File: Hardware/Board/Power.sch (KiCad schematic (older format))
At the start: 0 parts

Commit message: Schaltregler Design fertig gestellt, Datenblätter hinzu gefügt.
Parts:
- added C?: 22nF, symbol Device:C
- added C? (x5): 2u2, symbol Device:C
- added C? (x5): 100nF, symbol Device:C
- added C? (x4): 22uF, symbol Device:C
- added C?: 10uF, symbol Device:C
- added C? (x3): 5n6, symbol Device:C
- added C? (x2): 100n, symbol Device:C
- added C?: 4u7, symbol Device:C
- added C? (x2): 47u, symbol Device:C
- added C?: 1u, symbol Device:C
- added C?: 10u, symbol Device:C
- added F?: KFZ 5A, symbol Device:Fuse
- added L?: 10uH, symbol Device:L
- added L? (x3): 15uH, symbol Device:L
- added L?: L_Core_Ferrite, symbol Device:L_Core_Ferrite
- added Q? (x3): Q_NMOS_DGS, symbol Device:Q_NMOS_DGS
- added R?: 105k, symbol Device:R
- added R?: 22k6, symbol Device:R
- added R? (x2): 4r7, symbol Device:R
- added R? (x3): 10k, symbol Device:R
- added R? (x6): 40k2, symbol Device:R
- added R?: 178k, symbol Device:R
- added R?: 39k, symbol Device:R
- added R? (x2): 86k6, symbol Device:R
- added R? (x2): 32k4, symbol Device:R
- added R?: 432k, symbol Device:R
- added R?: 3M3, symbol Device:R
- added R?: 49k9, symbol Device:R
- added U? (x3): MAX17572, Package_DFN_QFN:DFN-12-1EP_3x3mm_P0.5mm_EP2.05x2.86mm, symbol Regulator_Switching:MAX17572
- added U?: MAX17574, Package_DFN_QFN:QFN-24-1EP_4x5mm_P0.5mm_EP2.65x3.65mm, symbol Regulator_Switching:MAX17574
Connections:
- new net: C?.2, U?.10 (BST) (x3)
- new net: C?.1, L?.1, U?.11 (LX) (x3)
- new net: R?.1, R?.2, U?.2 (EN/UVLO)
- new net: C?.1, U?.4 (SS) (x3)
- new net: R?.1, U?.6 (RT/SYNC) (x3)
- new net: R?.1, R?.2, U?.7 (FB) (x3)
- new net: Q?.1 (D), R?.2, U?.2 (EN/UVLO) (x2)
- new net: C?.2, U?.5 (VCC)
- new net: C?.1, R?.2, U?.9 (EXTVCC)
- new net: C?.1, L?.1, U?.1 (LX), U?.23 (LX), U?.24 (LX)
- new net: Q?.1 (D), R?.2, U?.10 (EN/UVLO)
- new net: C?.2, U?.12 (VCC)
- new net: C?.1, U?.16 (SS)
- new net: R?.1, R?.2, U?.18 (FB)
- new net: R?.1, U?.19 (RT)
- new net: R?.2, U?.20 (EXTVCC)
- new net: C?.2, U?.22 (BST)
- new net: Q?.2 (G), R?.1 (x3)
- new net: F?.2, L?.1
- new net +3.3VA: C?.1, L?.2, R?.1
- new net +3V3: C?.1, L?.2, R?.1
- new net +5V: C?.1, L?.2, R?.1, R?.1
- new net +5VD: C?.1, C?.1, C?.1, L?.2, R?.1, R?.1
- new net +BATT: C?.1, C?.1, C?.1, C?.1, C?.1, C?.1, C?.1, F?.1, R?.1, R?.1, R?.1, R?.1, U?.1 (VIN), U?.1 (VIN), U?.1 (VIN), U?.5 (VIN), U?.6 (VIN), U?.7 (VIN), U?.9 (VIN)
- new net 3VA_EN: R?.2
- new net 5V_EN: R?.2
- new net 5V_Raspi_EN: R?.2
- new net DC_Input: C?.1, C?.1, L?.2
- new net GND: C?.1, C?.1, C?.2, C?.2, C?.2, C?.2, C?.2, C?.2, C?.2, C?.2, C?.2, C?.2, C?.2, C?.2, C?.2, C?.2, C?.2, C?.2, C?.2, C?.2, C?.2, C?.2, Q?.3 (S), Q?.3 (S), Q?.3 (S), R?.2, R?.2, R?.2, R?.2, R?.2, R?.2, R?.2, R?.2, R?.2, U?.11 (PGND), U?.12 (PGND), U?.12 (PGND), U?.12 (PGND), U?.13 (EP), U?.13 (EP), U?.13 (EP), U?.2 (PGND), U?.21 (SGND), U?.25 (EP), U?.3 (PGND), U?.5 (VCC), U?.5 (VCC), U?.8 (GND), U?.8 (GND), U?.8 (GND), U?.9 (EXTVCC), U?.9 (EXTVCC)
- new net PWR_Reset: U?.3 (~RESET)
- no-connect marks 0 -> 4

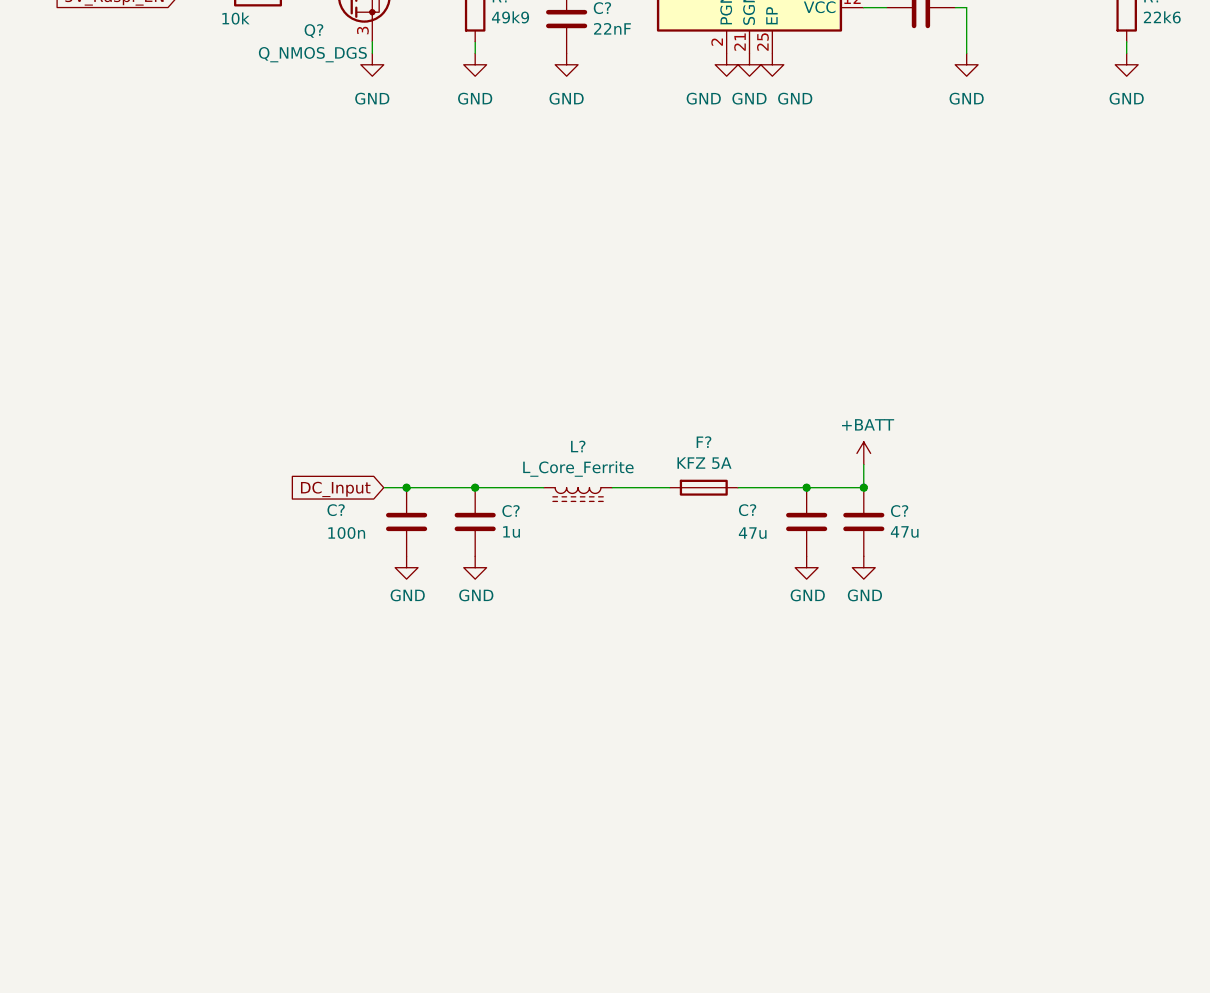
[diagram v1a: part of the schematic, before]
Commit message: FTDI EVE Touch hinzugefügt
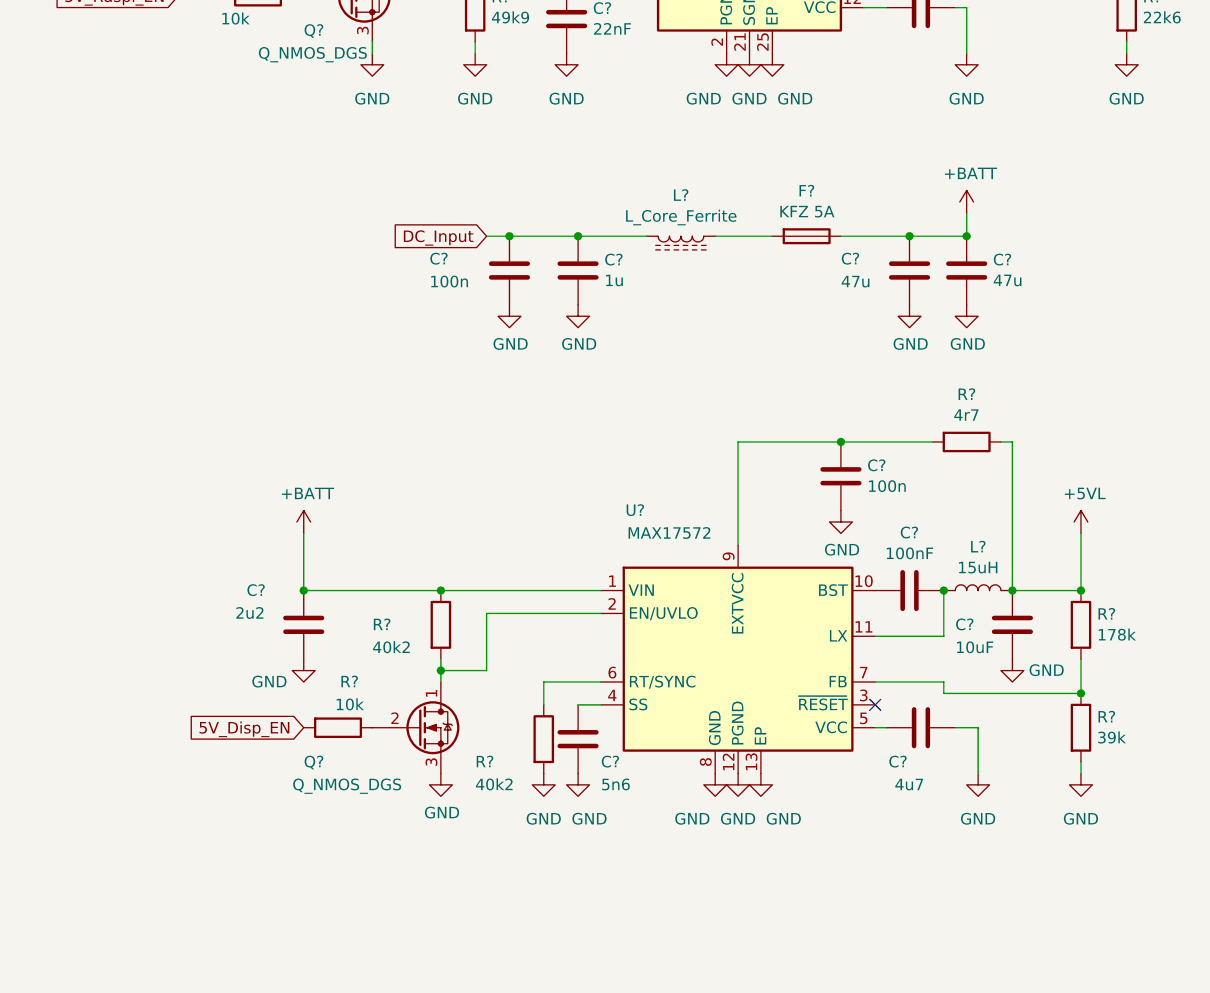
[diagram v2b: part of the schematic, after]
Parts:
- added C?: 10uF, symbol Device:C
- added C?: 5n6, symbol Device:C
- added C?: 100nF, symbol Device:C
- added C?: 2u2, symbol Device:C
- added C?: 100n, symbol Device:C
- added C?: 4u7, symbol Device:C
- added L?: 15uH, symbol Device:L
- added Q?: Q_NMOS_DGS, symbol Device:Q_NMOS_DGS
- added R?: 178k, symbol Device:R
- added R?: 39k, symbol Device:R
- added R? (x2): 40k2, symbol Device:R
- added R?: 4r7, symbol Device:R
- added R?: 10k, symbol Device:R
- added U?: MAX17572, Package_DFN_QFN:DFN-12-1EP_3x3mm_P0.5mm_EP2.05x2.86mm, symbol Regulator_Switching:MAX17572
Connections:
- net +BATT: now also C?.1, R?.1, U?.1 (VIN)
- net GND: now also C?.1, C?.2, C?.2, C?.2, C?.2, Q?.3 (S), R?.2, R?.2, U?.12 (PGND), U?.13 (EP), U?.8 (GND)
- new net: C?.1, L?.1, U?.11 (LX)
- new net: R?.1, R?.2, U?.7 (FB)
- new net: C?.1, U?.4 (SS)
- new net: C?.2, U?.10 (BST)
- new net: R?.1, U?.6 (RT/SYNC)
- new net: C?.1, R?.2, U?.9 (EXTVCC)
- new net: Q?.1 (D), R?.2, U?.2 (EN/UVLO)
- new net: C?.2, U?.5 (VCC)
- new net: Q?.2 (G), R?.1
- new net +5VL: C?.1, L?.2, R?.1, R?.1
- new net 5V_Disp_EN: R?.2
- no-connect marks 4 -> 5
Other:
- moved on the sheet: C?, F?, L?

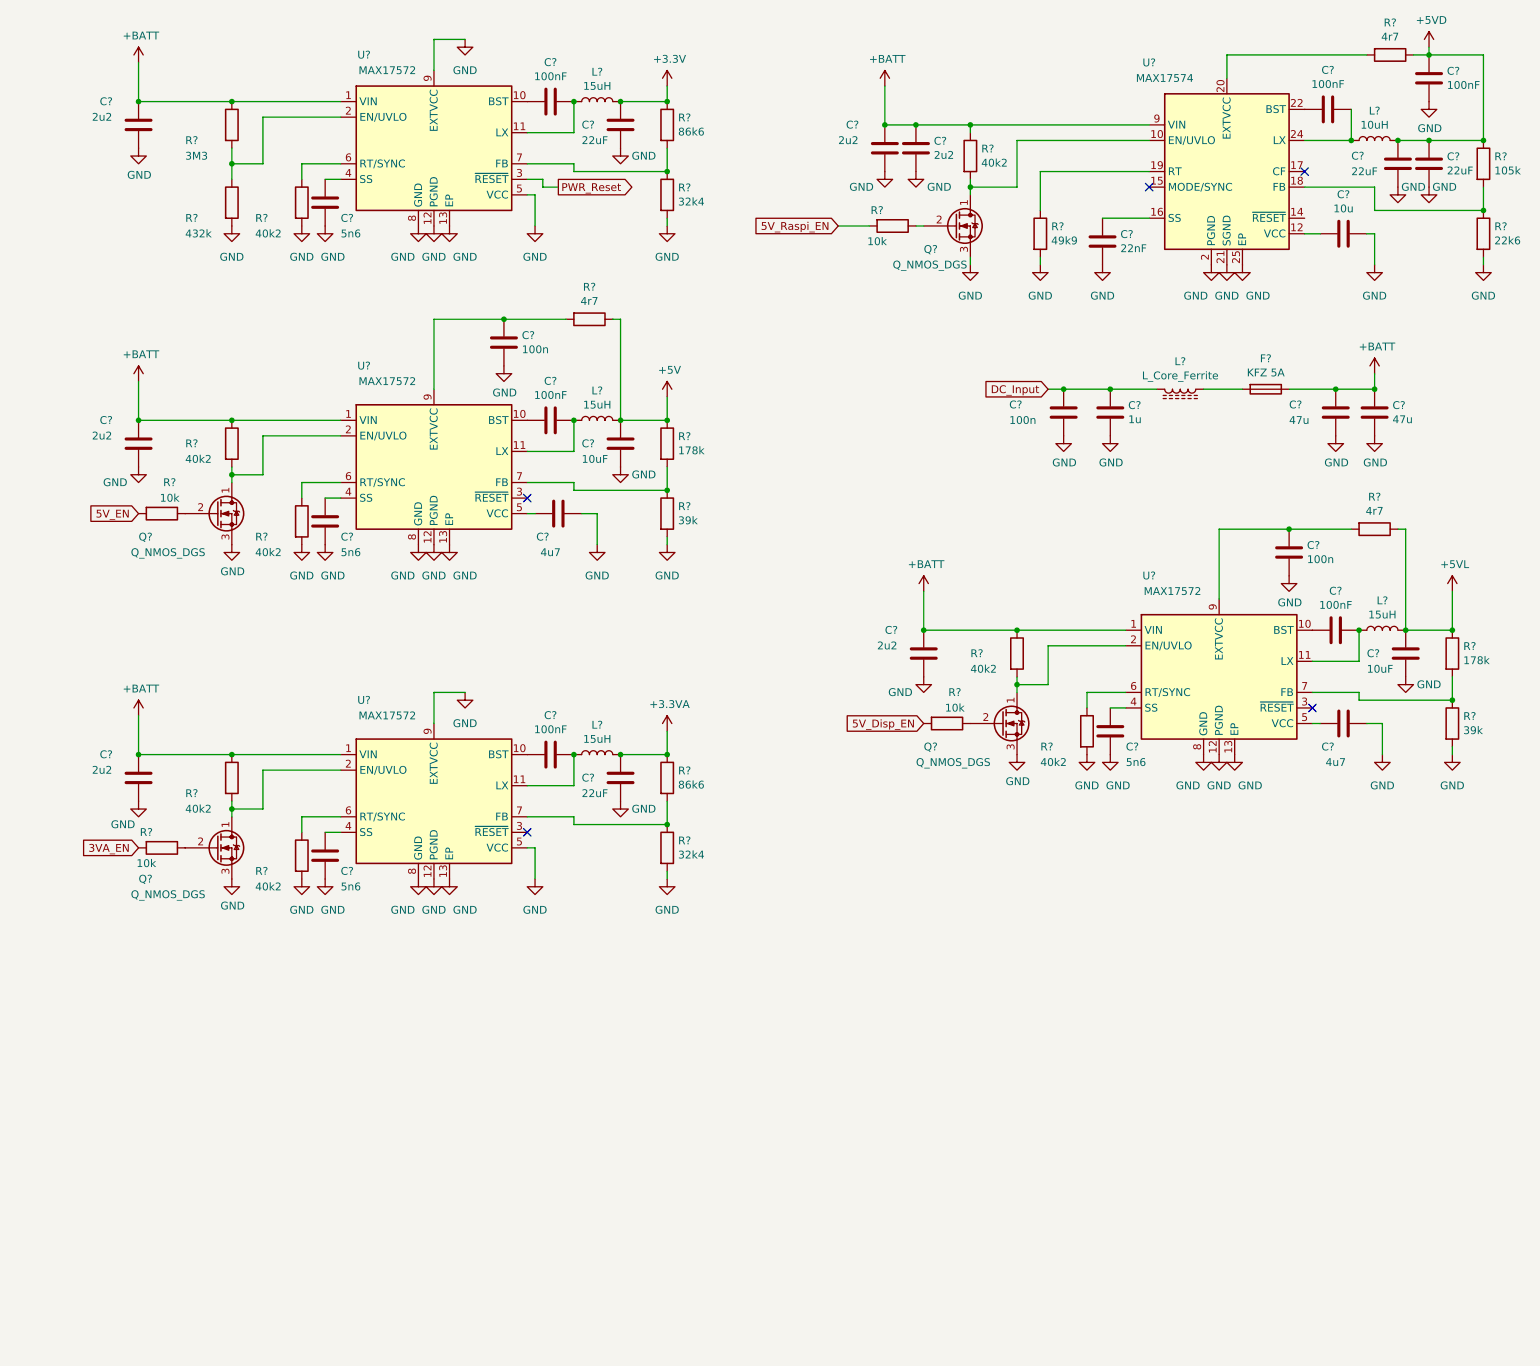
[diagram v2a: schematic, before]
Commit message: Netzliste und Board erstellt, hier sind noch Fehler im Bereich Footprints, BLE Modul nRF8001 hinzugefügt, erste Anschlussklemmen zugefügt
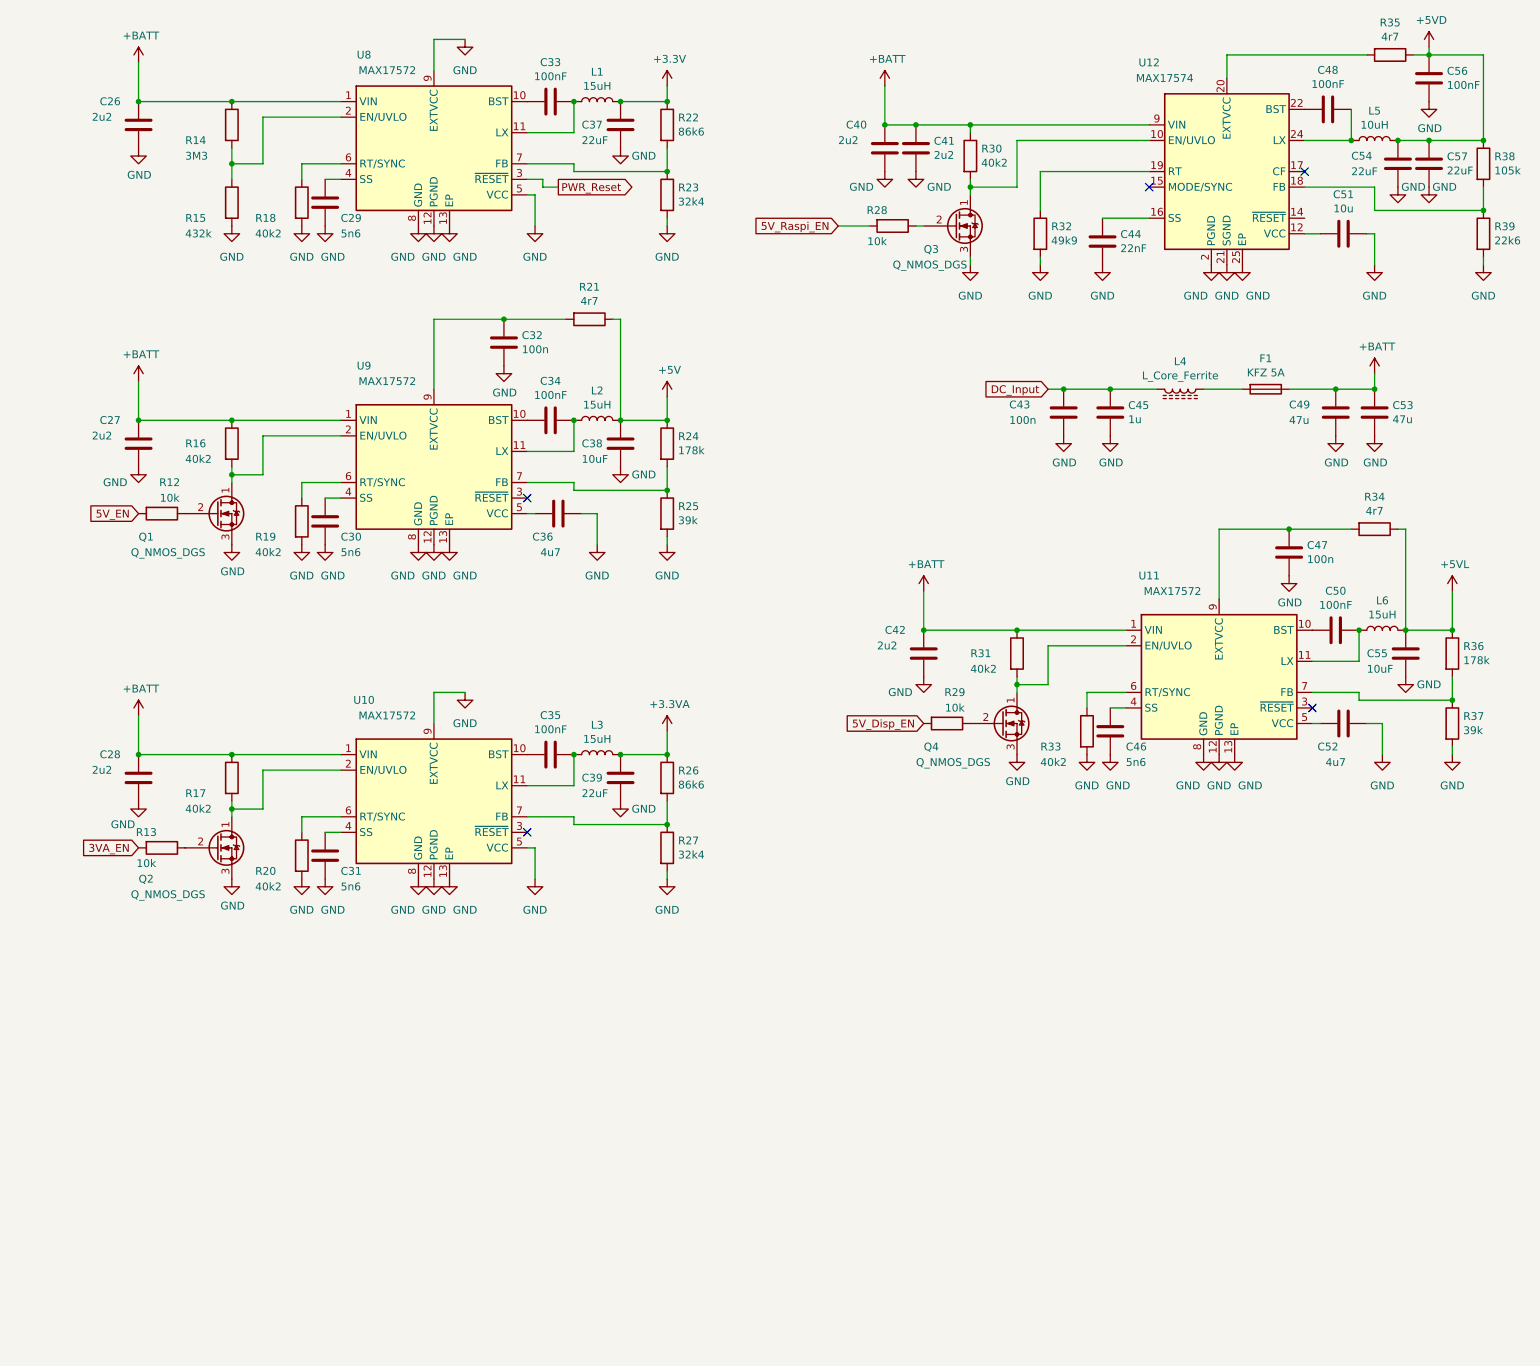
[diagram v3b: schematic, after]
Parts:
- C26, C27, C28, C29, C30, C31, C32, C33, C34, C35, C40, C41, C42, C43, C44, C45, C46, C47, C48, C50, C56: renamed from C?; footprint (none) -> Capacitor_SMD:C_0603_1608Metric
- C36, C37, C38, C39, C49, C51, C52, C53, C54, C55, C57: renamed from C?; footprint (none) -> Capacitor_SMD:C_1210_3225Metric
- F1: renamed from F?; footprint (none) -> Fuse:Fuseholder_Blade_ATO_Littelfuse_Pudenz_2_Pin
- R12, R13, R14, R15, R16, R17, R18, R19, R20, R21, R22, R23, R24, R25, R26, R27, R28, R29, R30, R31, R32, R33, R34, R35, R36, R37, R38, R39: renamed from R?; footprint (none) -> Resistor_SMD:R_0603_1608Metric
- gave numbers to parts that had none: 15
